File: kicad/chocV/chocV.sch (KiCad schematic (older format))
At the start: 82 parts, among them SW1 SW_Push, SW10 SW_Push, SW11 SW_Push, SW12 SW_Push, SW13 SW_Push, SW14 SW_Push, SW15 SW_Push, SW16 SW_Push, SW17 SW_Push, SW18 SW_Push, SW19 SW_Push, SW2 SW_Push, SW20 SW_Push, SW21 SW_Push, SW22 SW_Push, SW23 SW_Push, SW24 SW_Push, SW25 SW_Push, SW26 SW_Push, SW27 SW_Push, SW28 SW_Push, SW29 SW_Push, SW3 SW_Push, SW30 SW_Push, SW31 SW_Push, SW32 SW_Push, SW33 SW_Push, SW34 SW_Push, SW35 SW_Push, SW36 SW_Push, SW37 Reset Switch, SW4 SW_Push, SW5 SW_Push, SW6 SW_Push, SW7 SW_Push, SW8 SW_Push, SW9 SW_Push, U1 Pro-Micro

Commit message: Update PCB, top plate and bottom plate
Add Tactil switch TL3342
Add Slide switch MSK-12C02
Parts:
- added BT1: Device_Battery_Cell, other:PinHeader_1x02_P1.27mm_Vertical, symbol split_3x-cache:Device_Battery_Cell
- added SW38: Switch_SW_DIP_x01, other:switch_MSK-12C02_smd, symbol split_3x-cache:Switch_SW_DIP_x01
- SW1, SW10, SW11, SW12, SW13, SW14, SW15, SW16, SW17, SW18, SW19, SW2, SW20, SW21, SW22, SW23, SW24, SW25, SW26, SW27, SW28, SW29, SW3, SW30, SW31, SW32, SW33, SW34, SW35, SW36, SW4, SW5, SW6, SW7, SW8, SW9: symbol Switch:SW_Push -> chocV-rescue:SW_Push-Switch
- SW37: footprint Horizon:SW_Push_6mm -> other:SW_SPST_TL3342; symbol Switch:SW_Push -> chocV-rescue:SW_Push-Switch
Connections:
- net labels added: ground, raw
- wire segments 117 -> 119
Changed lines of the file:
@@
 reset
 $Comp
-L power:GND #PWR0101
+L chocV-rescue:GND-power #PWR0101
 U 1 1 61973D8F
 P 9700 4650
@@
 $EndComp
 $Comp
-L power:GND #PWR0102
-U 1 1 61974548
-P 8200 6100
-F 0 "#PWR0102" H 8200 5850 50  0001 C CNN
-F 1 "GND" H 8205 5927 50  0000 C CNN
-F 2 "" H 8200 6100 50  0001 C CNN
-F 3 "" H 8200 6100 50  0001 C CNN
-	1    8200 6100
-	1    0    0    -1
-$EndComp
-$Comp
-L Switch:SW_Push SW37
-U 1 1 61974F5B
-P 8400 6100
-F 0 "SW37" H 8400 6385 50  0000 C CNN
-F 1 "Reset Switch" H 8400 6294 50  0000 C CNN
-F 2 "Horizon:SW_Push_6mm" H 8400 6300 50  0001 C CNN
-F 3 "~" H 8400 6300 50  0001 C CNN
-	1    8400 6100
-	1    0    0    -1
-$EndComp
-Text GLabel 8600 6100 2    50   Input ~ 0
-reset
-$Comp
-L power:GND #PWR0103
+L chocV-rescue:GND-power #PWR0103
 U 1 1 61975D6B
 P 7400 4300
@@
 $EndComp
 $Comp
-L power:VCC #PWR0104
+L chocV-rescue:VCC-power #PWR0104
 U 1 1 619773E8
 P 7400 4750
@@
 	1600 1300 1600 1400
 $Comp
-L Switch:SW_Push SW1
+L chocV-rescue:SW_Push-Switch SW1
 U 1 1 61977F08
 P 1400 1300
@@
 	1600 2000 1600 2100
 $Comp
-L Switch:SW_Push SW11
+L chocV-rescue:SW_Push-Switch SW11
 U 1 1 6197E59D
 P 1400 2000
@@
 	1600 2700 1600 2800
 $Comp
-L Switch:SW_Push SW21
+L chocV-rescue:SW_Push-Switch SW21
 U 1 1 61980601
 P 1400 2700
@@
 	2400 1300 2400 1400
 $Comp
-L Switch:SW_Push SW2
+L chocV-rescue:SW_Push-Switch SW2
 U 1 1 61984D4C
 P 2200 1300
@@
 	2400 2000 2400 2100
 $Comp
-L Switch:SW_Push SW12
+L chocV-rescue:SW_Push-Switch SW12
 U 1 1 61984D59
 P 2200 2000
@@
 	2400 2700 2400 2800
 $Comp
-L Switch:SW_Push SW22
+L chocV-rescue:SW_Push-Switch SW22
 U 1 1 61984D66
 P 2200 2700
@@
 	3200 1300 3200 1400
 $Comp
-L Switch:SW_Push SW3
+L chocV-rescue:SW_Push-Switch SW3
 U 1 1 61987C29
 P 3000 1300
@@
 	3200 2000 3200 2100
 $Comp
-L Switch:SW_Push SW13
+L chocV-rescue:SW_Push-Switch SW13
 U 1 1 61987C36
 P 3000 2000
@@
 	3200 2700 3200 2800
 $Comp
-L Switch:SW_Push SW23
+L chocV-rescue:SW_Push-Switch SW23
 U 1 1 61987C43
 P 3000 2700
@@
 	4000 1300 4000 1400
 $Comp
-L Switch:SW_Push SW4
+L chocV-rescue:SW_Push-Switch SW4
 U 1 1 6198C8E5
 P 3800 1300
@@
 	4000 2000 4000 2100
 $Comp
-L Switch:SW_Push SW14
+L chocV-rescue:SW_Push-Switch SW14
 U 1 1 6198C8F2
 P 3800 2000
@@
 	4000 2700 4000 2800
 $Comp
-L Switch:SW_Push SW24
+L chocV-rescue:SW_Push-Switch SW24
 U 1 1 6198C8FF
 P 3800 2700
@@
 	4800 1300 4800 1400
 $Comp
-L Switch:SW_Push SW5
+L chocV-rescue:SW_Push-Switch SW5
 U 1 1 61993A90
 P 4600 1300
@@
 	4800 2000 4800 2100
 $Comp
-L Switch:SW_Push SW15
+L chocV-rescue:SW_Push-Switch SW15
 U 1 1 61993A9D
 P 4600 2000
@@
 	4800 2700 4800 2800
 $Comp
-L Switch:SW_Push SW25
+L chocV-rescue:SW_Push-Switch SW25
 U 1 1 61993AAA
 P 4600 2700
@@
 	6150 1300 6150 1400
 $Comp
-L Switch:SW_Push SW6
+L chocV-rescue:SW_Push-Switch SW6
 U 1 1 619B4BAA
 P 5950 1300
@@
 	6150 2000 6150 2100
 $Comp
-L Switch:SW_Push SW16
+L chocV-rescue:SW_Push-Switch SW16
 U 1 1 619B4BB7
 P 5950 2000
@@
 	6150 2700 6150 2800
 $Comp
-L Switch:SW_Push SW26
+L chocV-rescue:SW_Push-Switch SW26
 U 1 1 619B4BC4
 P 5950 2700
@@
 	6950 1300 6950 1400
 $Comp
-L Switch:SW_Push SW7
+L chocV-rescue:SW_Push-Switch SW7
 U 1 1 619B4BD1
 P 6750 1300
@@
 	6950 2000 6950 2100
 $Comp
-L Switch:SW_Push SW17
+L chocV-rescue:SW_Push-Switch SW17
 U 1 1 619B4BDE
 P 6750 2000
@@
 	6950 2700 6950 2800
 $Comp
-L Switch:SW_Push SW27
+L chocV-rescue:SW_Push-Switch SW27
 U 1 1 619B4BEB
 P 6750 2700
@@
 	7750 1300 7750 1400
 $Comp
-L Switch:SW_Push SW8
+L chocV-rescue:SW_Push-Switch SW8
 U 1 1 619B4BF8
 P 7550 1300
@@
 	7750 2000 7750 2100
 $Comp
-L Switch:SW_Push SW18
+L chocV-rescue:SW_Push-Switch SW18
 U 1 1 619B4C05
 P 7550 2000
@@
 	7750 2700 7750 2800
 $Comp
-L Switch:SW_Push SW28
+L chocV-rescue:SW_Push-Switch SW28
 U 1 1 619B4C12
 P 7550 2700
@@
 	8550 1300 8550 1400
 $Comp
-L Switch:SW_Push SW9
+L chocV-rescue:SW_Push-Switch SW9
 U 1 1 619B4C1F
 P 8350 1300
@@
 	8550 2000 8550 2100
 $Comp
-L Switch:SW_Push SW19
+L chocV-rescue:SW_Push-Switch SW19
 U 1 1 619B4C2C
 P 8350 2000
@@
 	8550 2700 8550 2800
 $Comp
-L Switch:SW_Push SW29
+L chocV-rescue:SW_Push-Switch SW29
 U 1 1 619B4C39
 P 8350 2700
@@
 	9350 1300 9350 1400
 $Comp
-L Switch:SW_Push SW10
+L chocV-rescue:SW_Push-Switch SW10
 U 1 1 619B4C46
 P 9150 1300
@@
 	9350 2000 9350 2100
 $Comp
-L Switch:SW_Push SW20
+L chocV-rescue:SW_Push-Switch SW20
 U 1 1 619B4C53
 P 9150 2000
@@
 	9350 2700 9350 2800
 $Comp
-L Switch:SW_Push SW30
+L chocV-rescue:SW_Push-Switch SW30
 U 1 1 619B4C60
 P 9150 2700
@@
 	4800 3400 4800 3500
 $Comp
-L Switch:SW_Push SW33
+L chocV-rescue:SW_Push-Switch SW33
 U 1 1 619B700C
 P 4600 3400
@@
 	4000 3400 4000 3500
 $Comp
-L Switch:SW_Push SW32
+L chocV-rescue:SW_Push-Switch SW32
 U 1 1 619B8267
 P 3800 3400
@@
 	3200 3400 3200 3500
 $Comp
-L Switch:SW_Push SW31
+L chocV-rescue:SW_Push-Switch SW31
 U 1 1 619B967E
 P 3000 3400
@@
 	7750 3400 7750 3500
 $Comp
-L Switch:SW_Push SW36
+L chocV-rescue:SW_Push-Switch SW36
 U 1 1 619BED4B
 P 7550 3400
@@
 	6950 3400 6950 3500
 $Comp
-L Switch:SW_Push SW35
+L chocV-rescue:SW_Push-Switch SW35
 U 1 1 619BED58
 P 6750 3400
@@
 	6150 3400 6150 3500
 $Comp
-L Switch:SW_Push SW34
+L chocV-rescue:SW_Push-Switch SW34
 U 1 1 619BED65
 P 5950 3400
@@
 Text GLabel 9300 4750 2    50   Input ~ 0
 row3
-$Comp
-L HorizonParts:Pro-Micro U1
-U 1 1 6197343E
-P 8600 4900
-F 0 "U1" H 8600 5737 60  0000 C CNN
-F 1 "Pro-Micro" H 8600 5631 60  0000 C CNN
-F 2 "Horizon:Pro-Micro" V 9650 2400 60  0001 C CNN
-F 3 "" V 9650 2400 60  0001 C CNN
-	1    8600 4900
-	-1   0    0    -1
-$EndComp
 Text GLabel 9300 4850 2    50   Input ~ 0
 row4
@@
 	1    0    0    -1
 $EndComp
+Text GLabel 8600 6100 2    50   Input ~ 0
+reset
+$Comp
+L chocV-rescue:SW_Push-Switch SW37
+U 1 1 61974F5B
+P 8400 6100
+F 0 "SW37" H 8400 6385 50  0000 C CNN
+F 1 "Reset Switch" H 8400 6294 50  0000 C CNN
+F 2 "other:SW_SPST_TL3342" H 8400 6300 50  0001 C CNN
+F 3 "~" H 8400 6300 50  0001 C CNN
+	1    8400 6100
+	1    0    0    -1
+$EndComp
+$Comp
+L chocV-rescue:GND-power #PWR0102
+U 1 1 61974548
+P 8200 6100
+F 0 "#PWR0102" H 8200 5850 50  0001 C CNN
+F 1 "GND" H 8205 5927 50  0000 C CNN
+F 2 "" H 8200 6100 50  0001 C CNN
+F 3 "" H 8200 6100 50  0001 C CNN
+	1    8200 6100
+	1    0    0    -1
+$EndComp
+$Comp
+L split_3x-cache:Device_Battery_Cell BT1
+U 1 1 61E7371F
+P 5200 5050
+F 0 "BT1" H 5318 5146 50  0000 L CNN
+F 1 "Device_Battery_Cell" H 5318 5055 50  0000 L CNN
+F 2 "other:PinHeader_1x02_P1.27mm_Vertical" V 5200 5110 50  0001 C CNN
+F 3 "" V 5200 5110 50  0001 C CNN
+	1    5200 5050
+	1    0    0    -1
+$EndComp
+$Comp
+L split_3x-cache:Switch_SW_DIP_x01 SW38
+U 1 1 61E78F9E
+P 6000 4650
+F 0 "SW38" H 6000 4917 50  0000 C CNN
+F 1 "Switch_SW_DIP_x01" H 6000 4826 50  0000 C CNN
+F 2 "other:switch_MSK-12C02_smd" H 6000 4650 50  0001 C CNN
+F 3 "" H 6000 4650 50  0001 C CNN
+	1    6000 4650
+	1    0    0    -1
+$EndComp
+Wire Wire Line
+	5200 4850 5200 4650
+Wire Wire Line
+	5200 4650 5700 4650
+Text GLabel 7900 4350 0    50   Input ~ 0
+raw
+$Comp
+L HorizonParts:Pro-Micro U1
+U 1 1 6197343E
+P 8600 4900
+F 0 "U1" H 8600 5737 60  0000 C CNN
+F 1 "Pro-Micro" H 8600 5631 60  0000 C CNN
+F 2 "Horizon:Pro-Micro" V 9650 2400 60  0001 C CNN
+F 3 "" V 9650 2400 60  0001 C CNN
+	1    8600 4900
+	-1   0    0    -1
+$EndComp
+Text GLabel 7900 4450 0    50   Input ~ 0
+ground
+Text GLabel 5200 5150 0    50   Input ~ 0
+ground
+Text GLabel 6300 4650 2    50   Input ~ 0
+raw
 $EndSCHEMATC

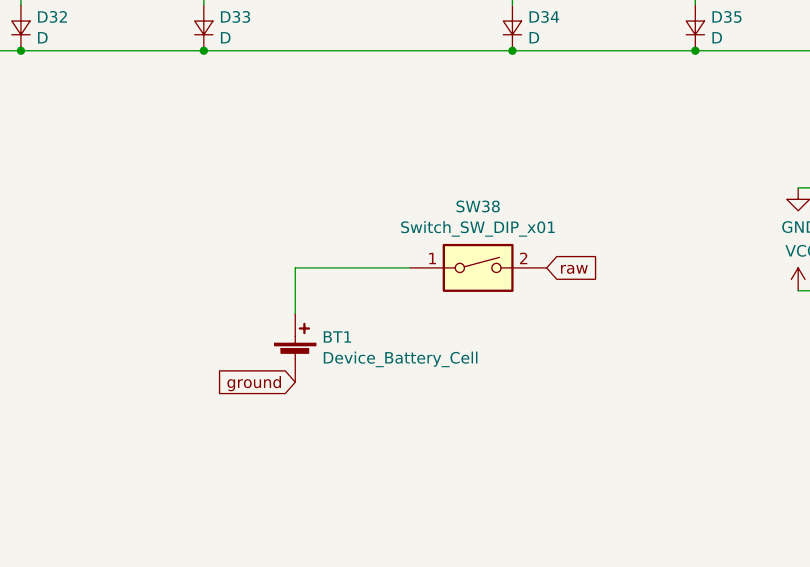
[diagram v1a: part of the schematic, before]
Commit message: Update PCB and Schematic
Add battery_pads
Switch PCB bottom side to ground plane
Move reset and power cut-off switches close to the border
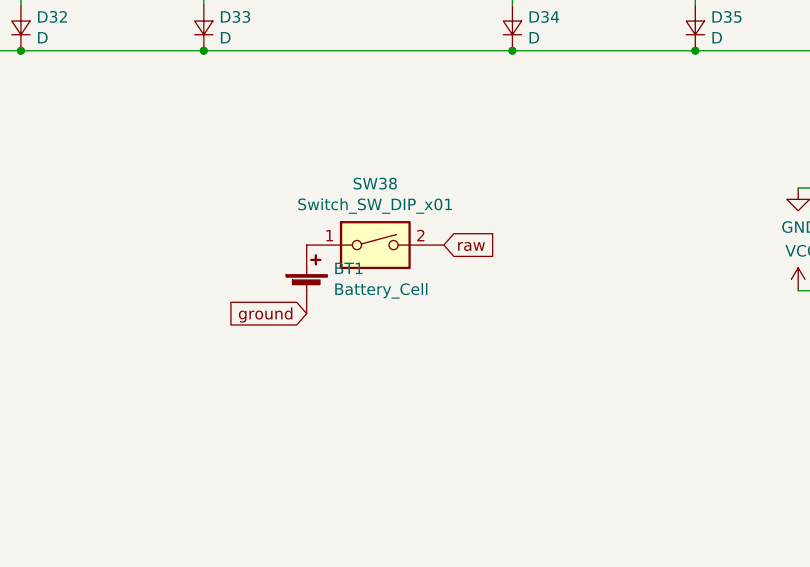
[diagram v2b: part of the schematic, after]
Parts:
- BT1: value Device_Battery_Cell -> Battery_Cell; footprint other:PinHeader_1x02_P1.27mm_Vertical -> other:battery_pads
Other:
- moved on the sheet: BT1, SW38
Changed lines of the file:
@@
 L split_3x-cache:Device_Battery_Cell BT1
 U 1 1 61E7371F
-P 5200 5050
-F 0 "BT1" H 5318 5146 50  0000 L CNN
-F 1 "Device_Battery_Cell" H 5318 5055 50  0000 L CNN
-F 2 "other:PinHeader_1x02_P1.27mm_Vertical" V 5200 5110 50  0001 C CNN
-F 3 "" V 5200 5110 50  0001 C CNN
-	1    5200 5050
+P 5250 4750
+F 0 "BT1" H 5368 4846 50  0000 L CNN
+F 1 "Battery_Cell" H 5368 4755 50  0000 L CNN
+F 2 "other:battery_pads" V 5250 4810 50  0001 C CNN
+F 3 "" V 5250 4810 50  0001 C CNN
+	1    5250 4750
 	1    0    0    -1
 $EndComp
@@
 L split_3x-cache:Switch_SW_DIP_x01 SW38
 U 1 1 61E78F9E
-P 6000 4650
-F 0 "SW38" H 6000 4917 50  0000 C CNN
-F 1 "Switch_SW_DIP_x01" H 6000 4826 50  0000 C CNN
-F 2 "other:switch_MSK-12C02_smd" H 6000 4650 50  0001 C CNN
-F 3 "" H 6000 4650 50  0001 C CNN
-	1    6000 4650
+P 5550 4550
+F 0 "SW38" H 5550 4817 50  0000 C CNN
+F 1 "Switch_SW_DIP_x01" H 5550 4726 50  0000 C CNN
+F 2 "other:switch_MSK-12C02_smd" H 5550 4550 50  0001 C CNN
+F 3 "" H 5550 4550 50  0001 C CNN
+	1    5550 4550
 	1    0    0    -1
 $EndComp
-Wire Wire Line
-	5200 4850 5200 4650
-Wire Wire Line
-	5200 4650 5700 4650
 Text GLabel 7900 4350 0    50   Input ~ 0
 raw
@@
 Text GLabel 7900 4450 0    50   Input ~ 0
 ground
-Text GLabel 5200 5150 0    50   Input ~ 0
+Text GLabel 5250 4850 0    50   Input ~ 0
 ground
-Text GLabel 6300 4650 2    50   Input ~ 0
+Text GLabel 5850 4550 2    50   Input ~ 0
 raw
 $EndSCHEMATC
